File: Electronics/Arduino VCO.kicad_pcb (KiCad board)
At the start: 2 copper layers, 61 parts, among them J5 Conn_02x08_Odd_Even, U1 TL072

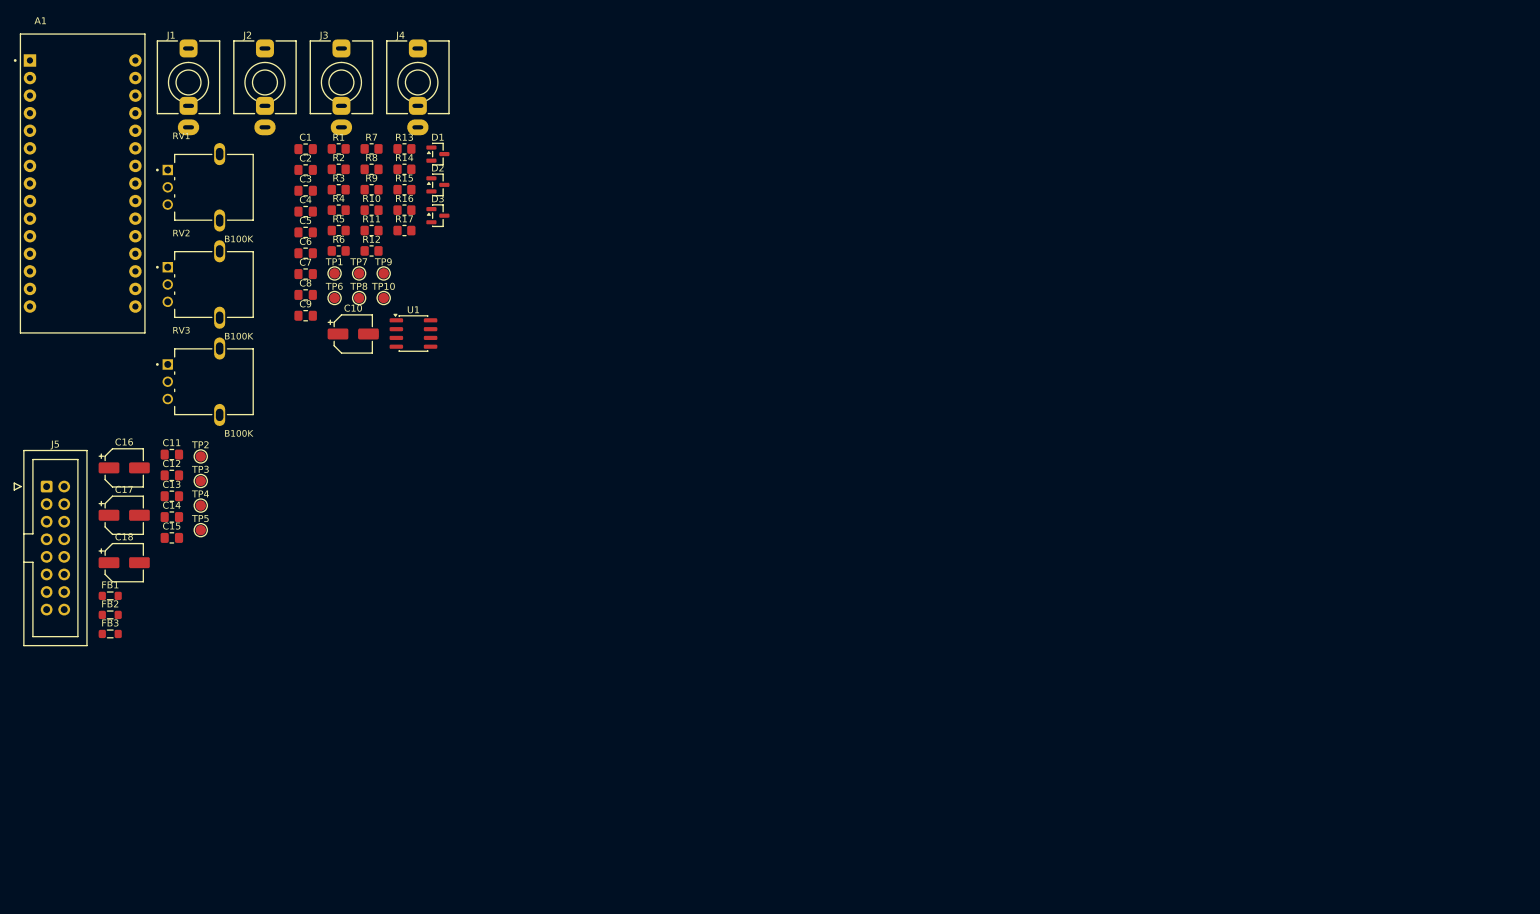
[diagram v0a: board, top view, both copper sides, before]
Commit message: Add font configuration file for KiCad CLI reports
This commit introduces a new `fonts.conf` file to specify font directories and cache location for the KiCad CLI reports. The configuration includes standard system font directories as well as a user-specific font directory.
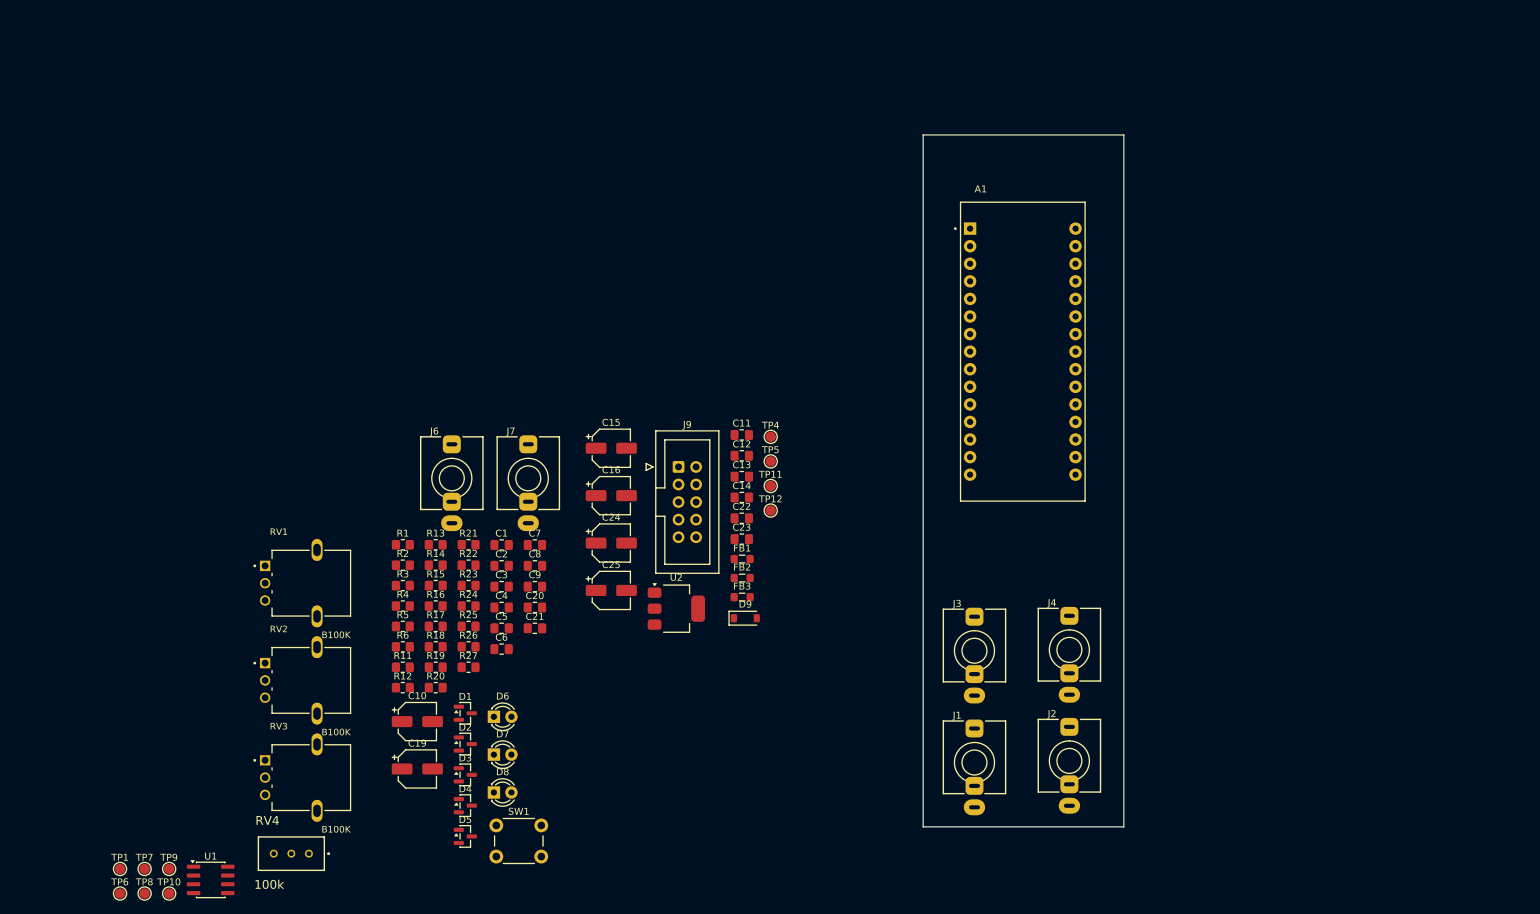
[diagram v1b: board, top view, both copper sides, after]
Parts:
- removed C17, C18: 10uF, Capacitor_SMD:CP_Elec_5x5.4
- removed J5: Conn_02x08_Odd_Even, Connector_IDC:IDC-Header_2x08_P2.54mm_Vertical
- removed R10, R8, R9: 100k, Resistor_SMD:R_0805_2012Metric_Pad1.20x1.40mm_HandSolder
- removed R7: 7k5, Resistor_SMD:R_0805_2012Metric_Pad1.20x1.40mm_HandSolder
- removed TP2: +5V, TestPoint:TestPoint_Pad_D1.5mm
- removed TP3: +12V, TestPoint:TestPoint_Pad_D1.5mm
- added C19: 10uF, Capacitor_SMD:CP_Elec_5x5.4, F.Cu at (89.0, 137.2)
- added C20: 100nF, Capacitor_SMD:C_0805_2012Metric_Pad1.18x1.45mm_HandSolder, F.Cu at (106.0, 113.8)
- added C21: 100nF, Capacitor_SMD:C_0805_2012Metric_Pad1.18x1.45mm_HandSolder, F.Cu at (106.0, 116.8)
- added C22: 100nF, Capacitor_SMD:C_0805_2012Metric_Pad1.18x1.45mm_HandSolder, F.Cu at (135.9, 100.9)
- added C23: 100nF, Capacitor_SMD:C_0805_2012Metric_Pad1.18x1.45mm_HandSolder, F.Cu at (135.9, 104.0)
- added C24: 10uF, Capacitor_SMD:CP_Elec_5x5.4, F.Cu at (117.0, 104.5)
- added C25: 10uF, Capacitor_SMD:CP_Elec_5x5.4, F.Cu at (117.0, 111.4)
- added D4: BAV99, Package_TO_SOT_SMD:SOT-23, F.Cu at (95.9, 142.5)
- added D5: BAV99, Package_TO_SOT_SMD:SOT-23, F.Cu at (95.9, 146.9)
- added D6: LED, LED_THT:LED_D3.0mm_IRBlack, F.Cu at (100.0, 129.6)
- added D7: LED, LED_THT:LED_D3.0mm_IRBlack, F.Cu at (100.0, 135.1)
- added D8: LED, LED_THT:LED_D3.0mm_IRBlack, F.Cu at (100.0, 140.6)
- added D9: 1N4148W, Diode_SMD:D_SOD-123, F.Cu at (136.4, 115.4)
- added J6: ~, Eurorack:Jack_3.5mm_QingPu_WQP-PJ398SM_Vertical, F.Cu at (94.0, 95.2)
- added J7: ~, Eurorack:Jack_3.5mm_QingPu_WQP-PJ398SM_Vertical, F.Cu at (105.0, 95.2)
- added J9: 10-pin power header, Connector_IDC:IDC-Header_2x05_P2.54mm_Vertical, F.Cu at (126.7, 93.5)
- added R18: 47k, Resistor_SMD:R_0805_2012Metric_Pad1.20x1.40mm_HandSolder, F.Cu at (91.6, 119.5)
- added R19: 1k, Resistor_SMD:R_0805_2012Metric_Pad1.20x1.40mm_HandSolder, F.Cu at (91.6, 122.5)
- added R20: 100k, Resistor_SMD:R_0805_2012Metric_Pad1.20x1.40mm_HandSolder, F.Cu at (91.6, 125.4)
- added R21: 50k, Resistor_SMD:R_0805_2012Metric_Pad1.20x1.40mm_HandSolder, F.Cu at (96.4, 104.8)
- added R22: 50k, Resistor_SMD:R_0805_2012Metric_Pad1.20x1.40mm_HandSolder, F.Cu at (96.4, 107.7)
- added R23: 1k, Resistor_SMD:R_0805_2012Metric_Pad1.20x1.40mm_HandSolder, F.Cu at (96.4, 110.7)
- added R24: 100k, Resistor_SMD:R_0805_2012Metric_Pad1.20x1.40mm_HandSolder, F.Cu at (96.4, 113.6)
- added R25: 1k, Resistor_SMD:R_0805_2012Metric_Pad1.20x1.40mm_HandSolder, F.Cu at (96.4, 116.6)
- added R26: 1k, Resistor_SMD:R_0805_2012Metric_Pad1.20x1.40mm_HandSolder, F.Cu at (96.4, 119.5)
- added R27: 1k, Resistor_SMD:R_0805_2012Metric_Pad1.20x1.40mm_HandSolder, F.Cu at (96.4, 122.5)
- added RV4: 100k, Eurorack:Trimmer_Bourns_3296W_50k_THT, F.Cu at (73.3, 149.4)
- added SW1: MODE, Button_Switch_THT:SW_PUSH_6mm, F.Cu at (100.4, 145.3)
- added TP11: +5V, TestPoint:TestPoint_Pad_D1.5mm, F.Cu at (140.0, 96.3)
- added TP12: +12V, TestPoint:TestPoint_Pad_D1.5mm, F.Cu at (140.0, 99.8)
- added U2: AMS1117-5.0, Package_TO_SOT_SMD:SOT-223-3_TabPin2, F.Cu at (126.4, 114.0)
- C1: value 22nF -> 4.7nF
- C15: value 100nF -> 10uF; footprint Capacitor_SMD:C_0805_2012Metric_Pad1.18x1.45mm_HandSolder -> Capacitor_SMD:CP_Elec_5x5.4
- C5: value 3.3nF -> 10nF
- C6, C7, C8: value 68n -> 100nF
- R6: value 2k7 -> 3.9k
- TP4: value GND -> -12V
- TP5: value -12V -> GND
- moved J2 152.1 mm to (183.2, 136.0)
- moved J1 150.2 mm to (169.5, 136.2)
- moved A1 138.0 mm to (176.5, 76.9)
- moved J4 124.9 mm to (183.2, 120.0)
- moved J3 122.9 mm to (169.5, 120.1)
- moved FB1 91.5 mm to (135.9, 106.8)
- moved FB2 91.5 mm to (135.9, 109.6)
- moved FB3 91.5 mm to (135.9, 112.3)
- moved TP1 91.5 mm to (46.0, 151.6)
- moved TP7 91.5 mm to (49.6, 151.6)
- moved TP9 91.5 mm to (53.1, 151.6)
- moved TP10 91.5 mm to (53.1, 155.2)
- moved TP6 91.5 mm to (46.0, 155.2)
- moved TP8 91.5 mm to (49.6, 155.2)
- moved U1 84.2 mm to (59.1, 153.2)
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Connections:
- A1 pad 10: unconnected-(A1-D7-Pad10) -> LED 2
- A1 pad 11: unconnected-(A1-D8-Pad11) -> LED 3
- A1 pad 21: unconnected-(A1-A2-Pad21) -> CV 4
- A1 pad 25: unconnected-(A1-A6-Pad25) -> GAIN CV
- A1 pad 7: unconnected-(A1-D4-Pad7) -> Net-(A1-D4)
- A1 pad 9: unconnected-(A1-D6-Pad9) -> LED 1
- C13 pad 1: +5V -> +12V
- C14 pad 1: +12V -> GND
- C14 pad 2: GND -> -12V
- C15 pad 1: GND -> +12V
- C15 pad 2: -12V -> GND
- C16 pad 1: +5V -> GND
- C16 pad 2: GND -> -12V
- C5 pad 1: Net-(C5-Pad1) -> Net-(U1A-+)
- C5 pad 2: Net-(U1A--) -> GND
- FB1 pad 1: +5V -> Net-(D9-K)
- FB1 pad 2: Net-(J5-Pin_11) -> +12V
- R11 pad 1: Net-(R10-Pad2) -> Net-(C19-Pad1)
- R6 pad 2: Net-(U1A--) -> Net-(U1A-+)
- TP4 pad 1: GND -> -12V
- TP5 pad 1: -12V -> GND
- TP9 pad 1: Net-(R10-Pad2) -> Net-(C19-Pad1)
- U1 pad 1: Net-(C5-Pad1) -> Net-(C19-Pad1)
- U1 pad 3: GND -> Net-(U1A-+)
- U1 pad 7: Net-(R10-Pad2) -> Net-(U1B--)
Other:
- board outline added: 29 x 100 mm

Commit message: starting pcb
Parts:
- removed C10: 10uF, Capacitor_SMD:CP_Elec_5x5.4
- removed C22, C9: 100nF, Capacitor_SMD:C_0805_2012Metric_Pad1.18x1.45mm_HandSolder
- removed FB1: FerriteBead_Small, Inductor_SMD:L_0805_2012Metric_Pad1.05x1.20mm_HandSolder
- removed TP1: A, TestPoint:TestPoint_Pad_D1.5mm
- A1, C1, C11, C12, C13, C15, C19, C2, C20, C23, C25, C3, C4, C5, D4, D9, FB2, J9, R1, R11, R18, R19, R2, R20, R21, R22, R3, R4, R5, R6, TP10, TP11, TP12, TP4, TP5, TP6, TP7, TP8, TP9, U1, U2: moved to B.Cu
- C24: value 10uF -> 100nF; footprint Capacitor_SMD:CP_Elec_5x5.4 -> Capacitor_SMD:C_0805_2012Metric_Pad1.18x1.45mm_HandSolder; moved to B.Cu
- D6, D7, D8: footprint LED_THT:LED_D3.0mm_IRBlack -> LED_THT:LED_D3.0mm_Clear
- SW1: footprint Button_Switch_THT:SW_PUSH_6mm -> Button_Switch_THT:SW_PUSH_6mm_H13mm
- moved TP6 197.7 mm to (220.5, 62.3), turned to 180 degrees
- moved TP10 196.5 mm to (220.6, 52.5), turned to 180 degrees
- moved TP7 194.9 mm to (220.6, 58.1), turned to 180 degrees
- moved TP9 180.1 mm to (230.6, 121.0), turned to 180 degrees
- moved RV4 179.4 mm to (243.6, 93.0)
- moved TP8 177.4 mm to (224.4, 125.2), turned to 180 degrees
- moved RV2 173.8 mm to (232.5, 52.1), turned to 90 degrees
- moved RV3 173.2 mm to (232.5, 67.6), turned to 90 degrees
- moved U1 171.2 mm to (220.9, 97.3), turned to -90 degrees
- moved RV1 160.3 mm to (232.5, 83.1), turned to 90 degrees
- moved R4 157.6 mm to (235.7, 61.8)
- moved R5 153.7 mm to (233.8, 71.5)
- moved R14 153.3 mm to (244.3, 121.7), turned to 90 degrees
- moved R15 153.1 mm to (244.7, 108.9)
- moved D1 150.7 mm to (244.7, 105.2)
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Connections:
- C24 pad 1: Net-(D9-K) -> +12V
- D9 pad 1: Net-(D9-K) -> +12V
- U2 pad 3: Net-(D9-K) -> +12V
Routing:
- net +5V: track 0.00 -> 154.5 mm, vias 0 -> 4
- net CV 4: track 0.00 -> 92.5 mm, vias 0 -> 1
- net Net-(C19-Pad1): track 0.00 -> 77.4 mm, vias 0 -> 5
- net GAIN CV: track 0.00 -> 76.8 mm, vias 0 -> 1
- net CV 2: track 0.00 -> 69.1 mm, vias 0 -> 1
- net CV 1: track 0.00 -> 66.3 mm, vias 0 -> 3
- net CV 3: track 0.00 -> 65.1 mm, vias 0 -> 3
- net +12V: track 0.00 -> 61.0 mm, vias 0 -> 2
- net Net-(A1-D4): track 0.00 -> 47.5 mm, vias 0 -> 1
- net Net-(D8-A): track 0.00 -> 39.6 mm, vias 0 -> 1
- net -12V: track 0.00 -> 31.8 mm, vias 0 -> 2
- net Net-(D7-A): track 0.00 -> 31.6 mm, vias 0 -> 1
- net Net-(U1A--): track 0.00 -> 25.8 mm, vias 0 -> 1
- net Out 2: track 0.00 -> 24.8 mm
- net Net-(J4-PadT): track 0.00 -> 23.7 mm
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- added copper zone on B.Cu, net GND
- added copper zone on F.Cu, net GND
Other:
- outline, holes or cut-outs redrawn

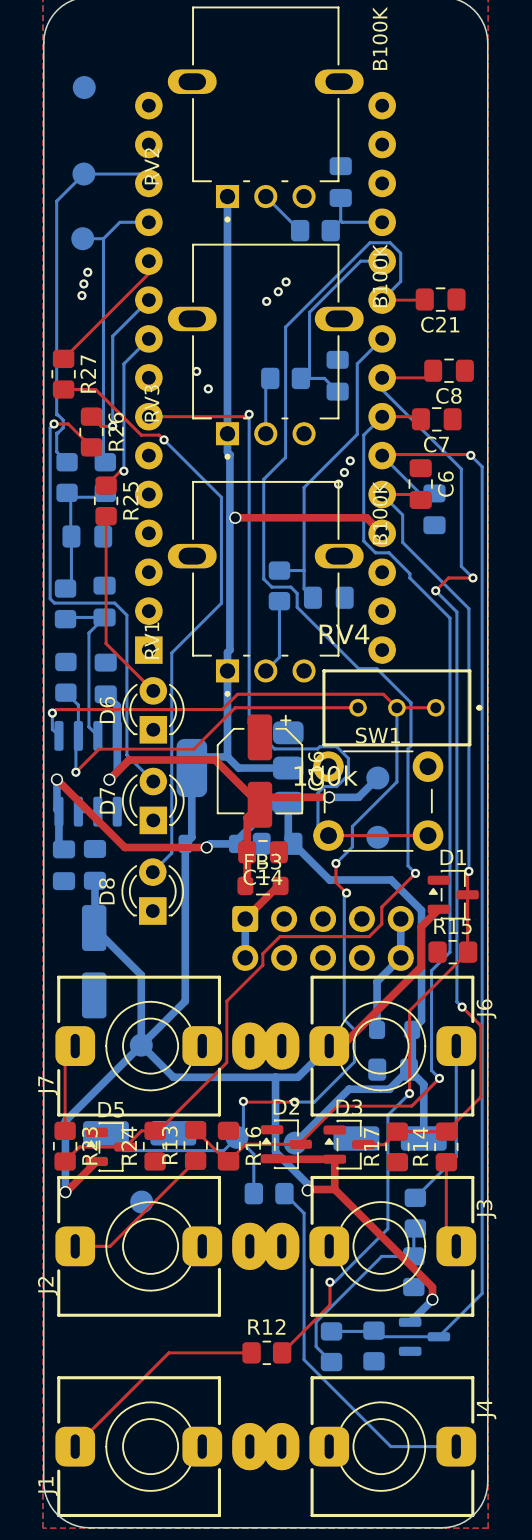
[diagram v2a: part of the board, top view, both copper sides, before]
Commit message: changing tracks
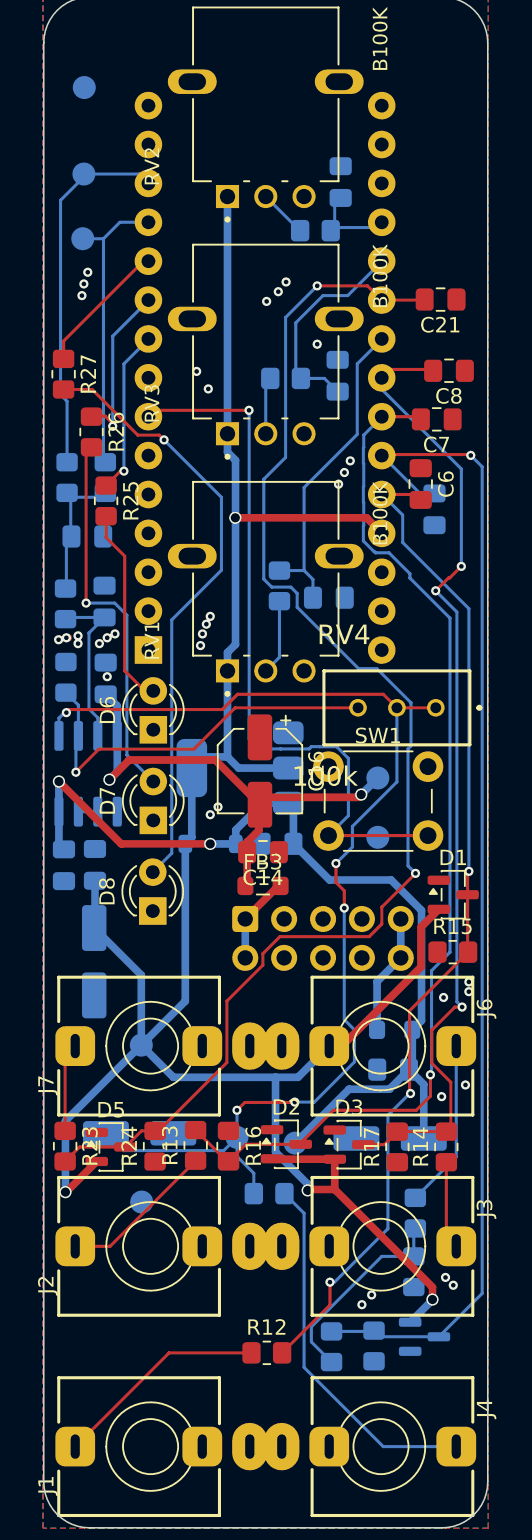
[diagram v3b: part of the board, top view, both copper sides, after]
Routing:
- net Net-(D7-A): track 31.6 -> 24.9 mm
- net CV 4: track 92.5 -> 87.0 mm, vias 1 -> 2
- net CV 3: track 65.1 -> 64.0 mm
- net Net-(C19-Pad1): track 77.4 -> 76.3 mm
- net +5V: track 154.5 -> 153.7 mm
- net Out 2: track 24.8 -> 24.1 mm
- net KNOB 2: track 13.2 -> 13.8 mm
- net GND: track 0.00 -> 0.13 mm, vias 11 -> 35

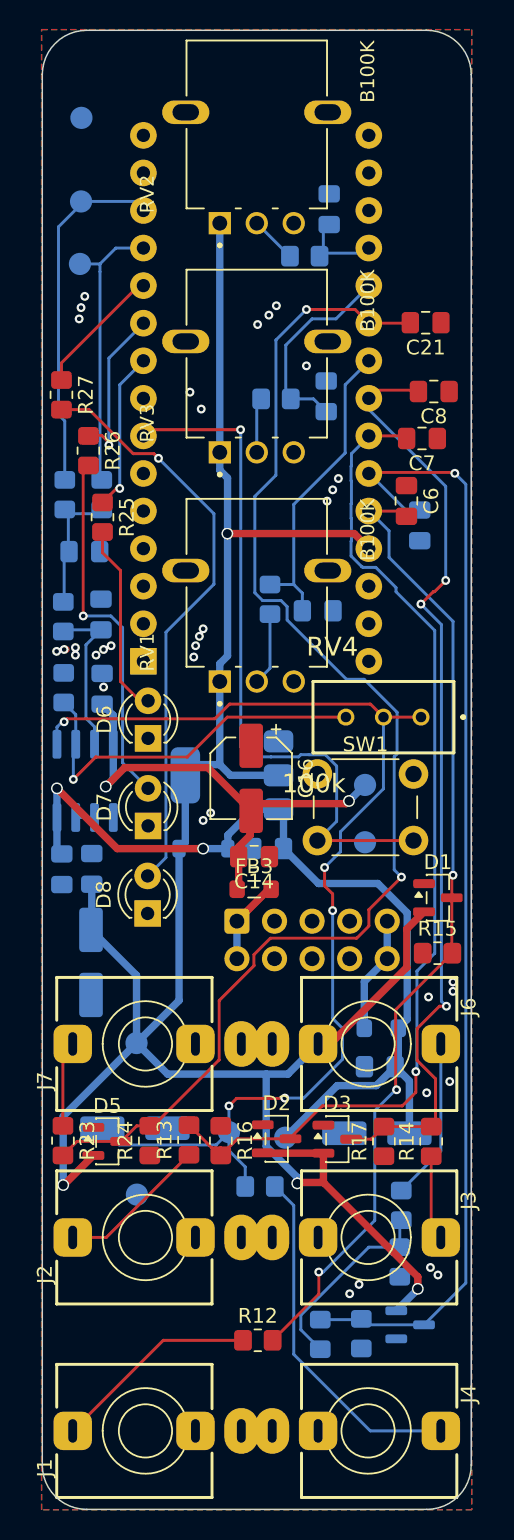
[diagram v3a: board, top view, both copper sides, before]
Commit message: finishing tracks and resolving drc errors
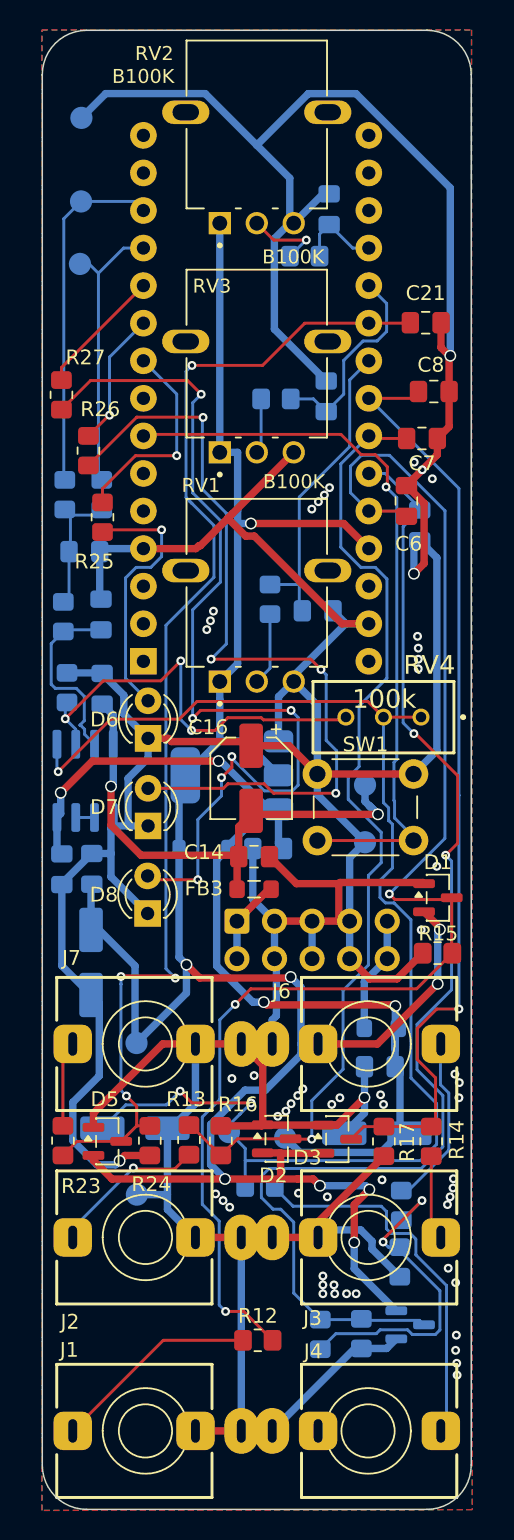
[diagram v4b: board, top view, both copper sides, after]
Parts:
- SW1: footprint Button_Switch_THT:SW_PUSH_6mm_H13mm -> Eurorack:SW_PUSH_6mm_H13mm_1
- moved R18 0.22 mm to (219.7, 91.0)
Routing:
- net GND: track 0.13 -> 389.2 mm, vias 35 -> 57
- net Net-(D7-A): track 24.9 -> 56.2 mm, vias 1 -> 4
- net CV 1: track 66.4 -> 92.6 mm
- net Net-(D8-A): track 39.6 -> 64.9 mm, vias 1 -> 6
- net Net-(C19-Pad1): track 76.3 -> 91.8 mm, vias 5 -> 3
- net +5V: track 153.7 -> 163.7 mm, vias 4 -> 9
- net Net-(R19-Pad1): track 13.3 -> 22.7 mm, vias 0 -> 2
- net +12V: track 60.9 -> 69.0 mm, vias 2 -> 4
- net GAIN CV: track 76.8 -> 83.8 mm, vias 1 -> 2
- net CV 4: track 87.0 -> 81.2 mm, vias 2 -> 4
- net Net-(D6-A): track 13.0 -> 17.8 mm, vias 0 -> 1
- net -12V: track 31.8 -> 36.3 mm
- net LED 1: track 10.9 -> 14.2 mm
- net Net-(A1-D4): track 47.4 -> 50.2 mm
- net Net-(U1A--): track 25.8 -> 28.5 mm, vias 1 -> 3
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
